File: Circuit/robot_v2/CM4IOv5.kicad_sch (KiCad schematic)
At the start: 1 part, among them J18 Conn_01x12_Pin

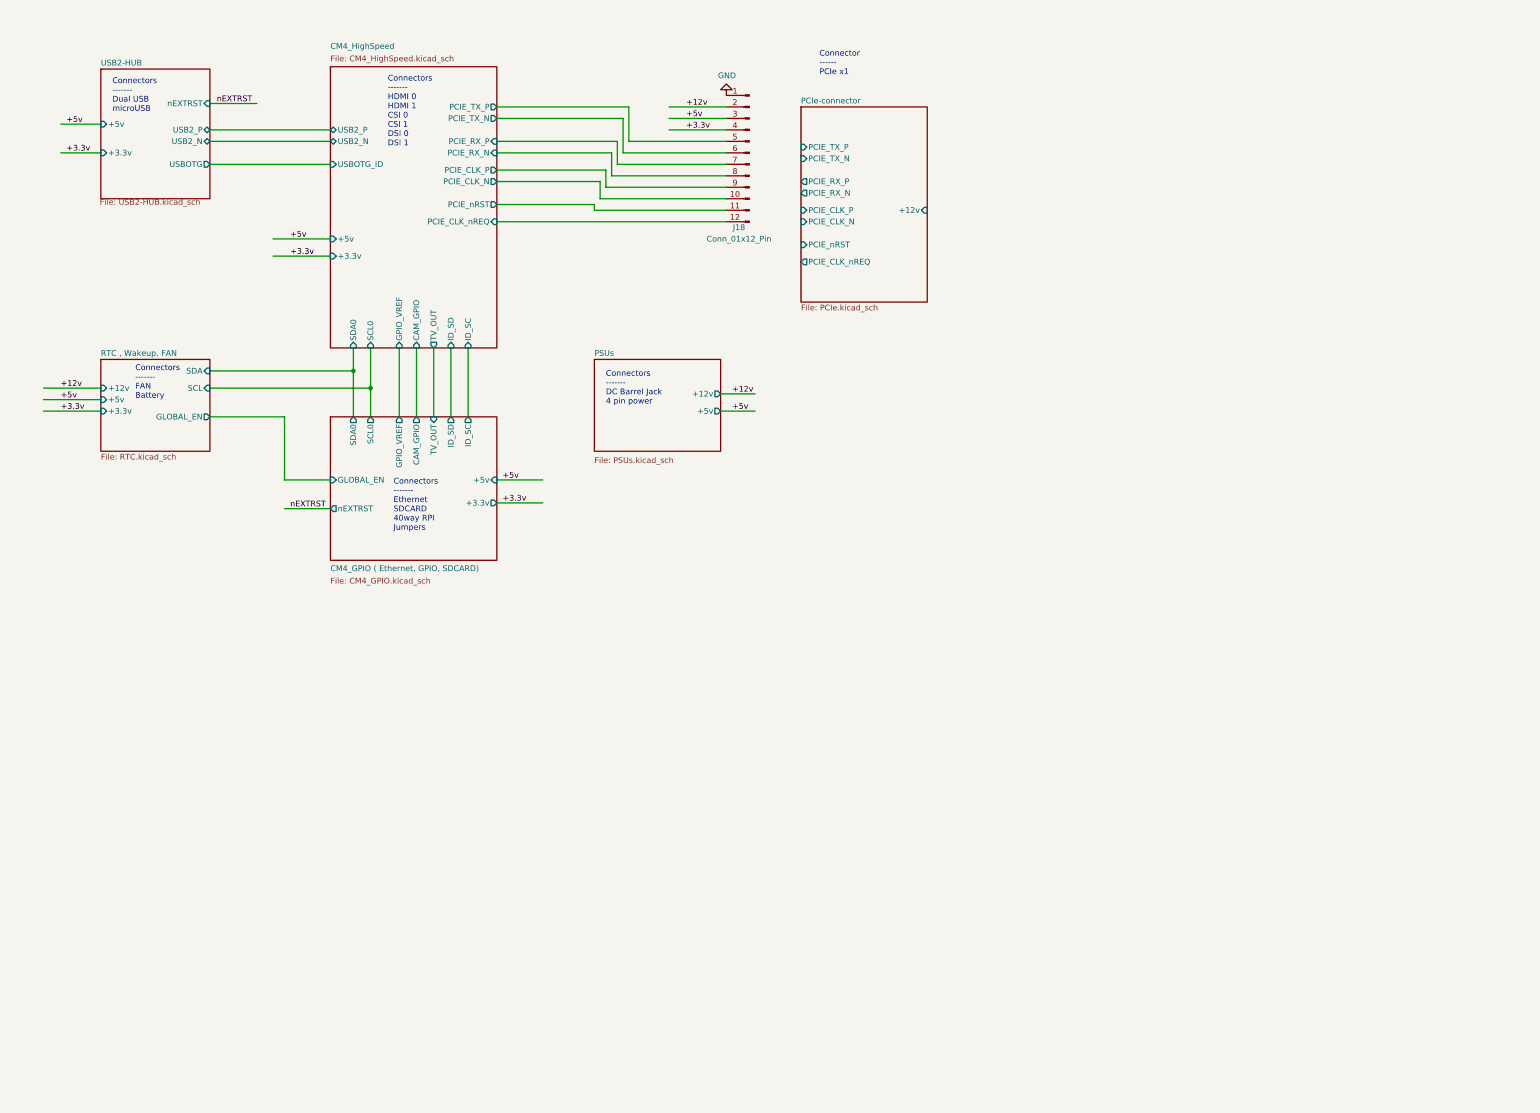
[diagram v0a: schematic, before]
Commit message: feat(kicad): Advance PCB to v0.3 and add EV3 color sensor test
Updates the main robot PCB design to version 0.3 ('Robot fő nyák_v3') with new features and refinements. Simultaneously adds a v0.1 test program for the Lego EV3 color sensor.
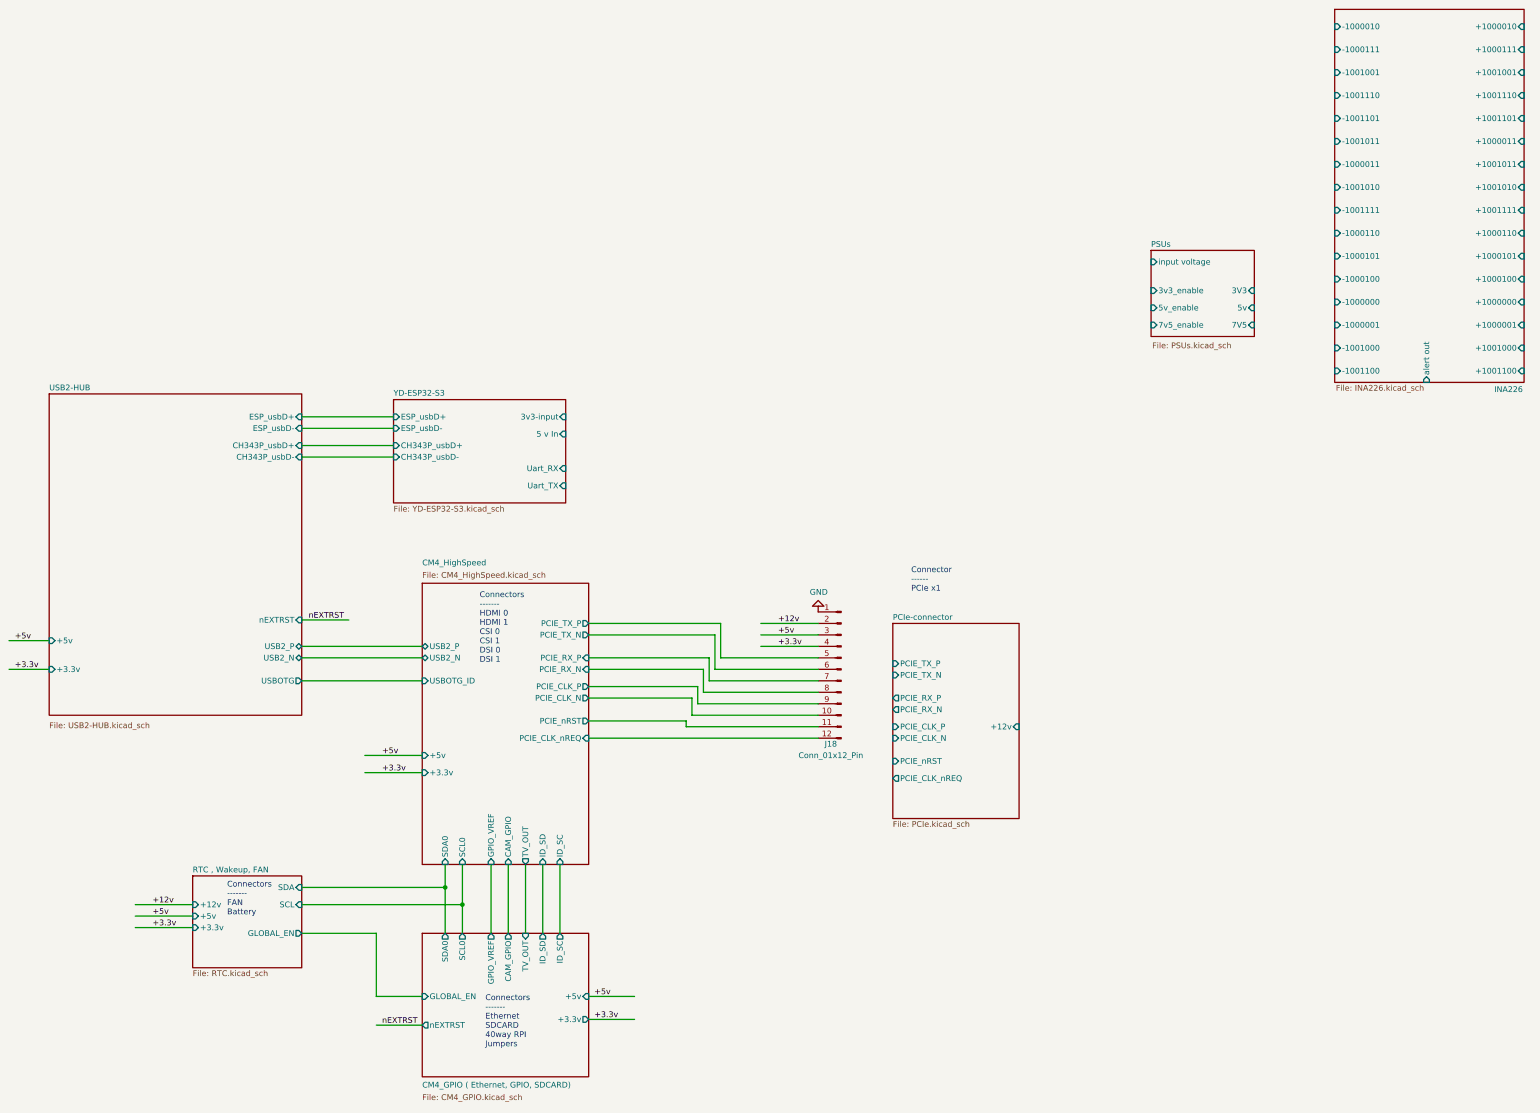
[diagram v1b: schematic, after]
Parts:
- J18: footprint Connector_JST:JST_EH_B12B-EH-A_1x12_P2.50mm_Vertical -> Connector_PinHeader_2.54mm:PinHeader_1x12_P2.54mm_Vertical
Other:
- added sheet INA226 (INA226.kicad_sch)
- added sheet YD-ESP32-S3 (YD-ESP32-S3.kicad_sch)
- sheet PSUs ports: added 3V3, 3v3_enable, 5v, 5v_enable, 7V5, 7v5_enable, input voltage; removed +12v, +5v
- sheet USB2-HUB ports: added CH343P_usbD+, CH343P_usbD-, ESP_usbD+, ESP_usbD-; removed none
- note removed: "Connectors ------- DC Barrel Jack 4 pin power"
- note removed: "Connectors ------- Dual USB microUSB"
- moved on the sheet: J18

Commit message: chore: Update web page and save KiCad progress
This commit includes miscellaneous updates. The project's webpage (`web/index.html`) has been modified, and various KiCad project files have been saved, reflecting ongoing design work.
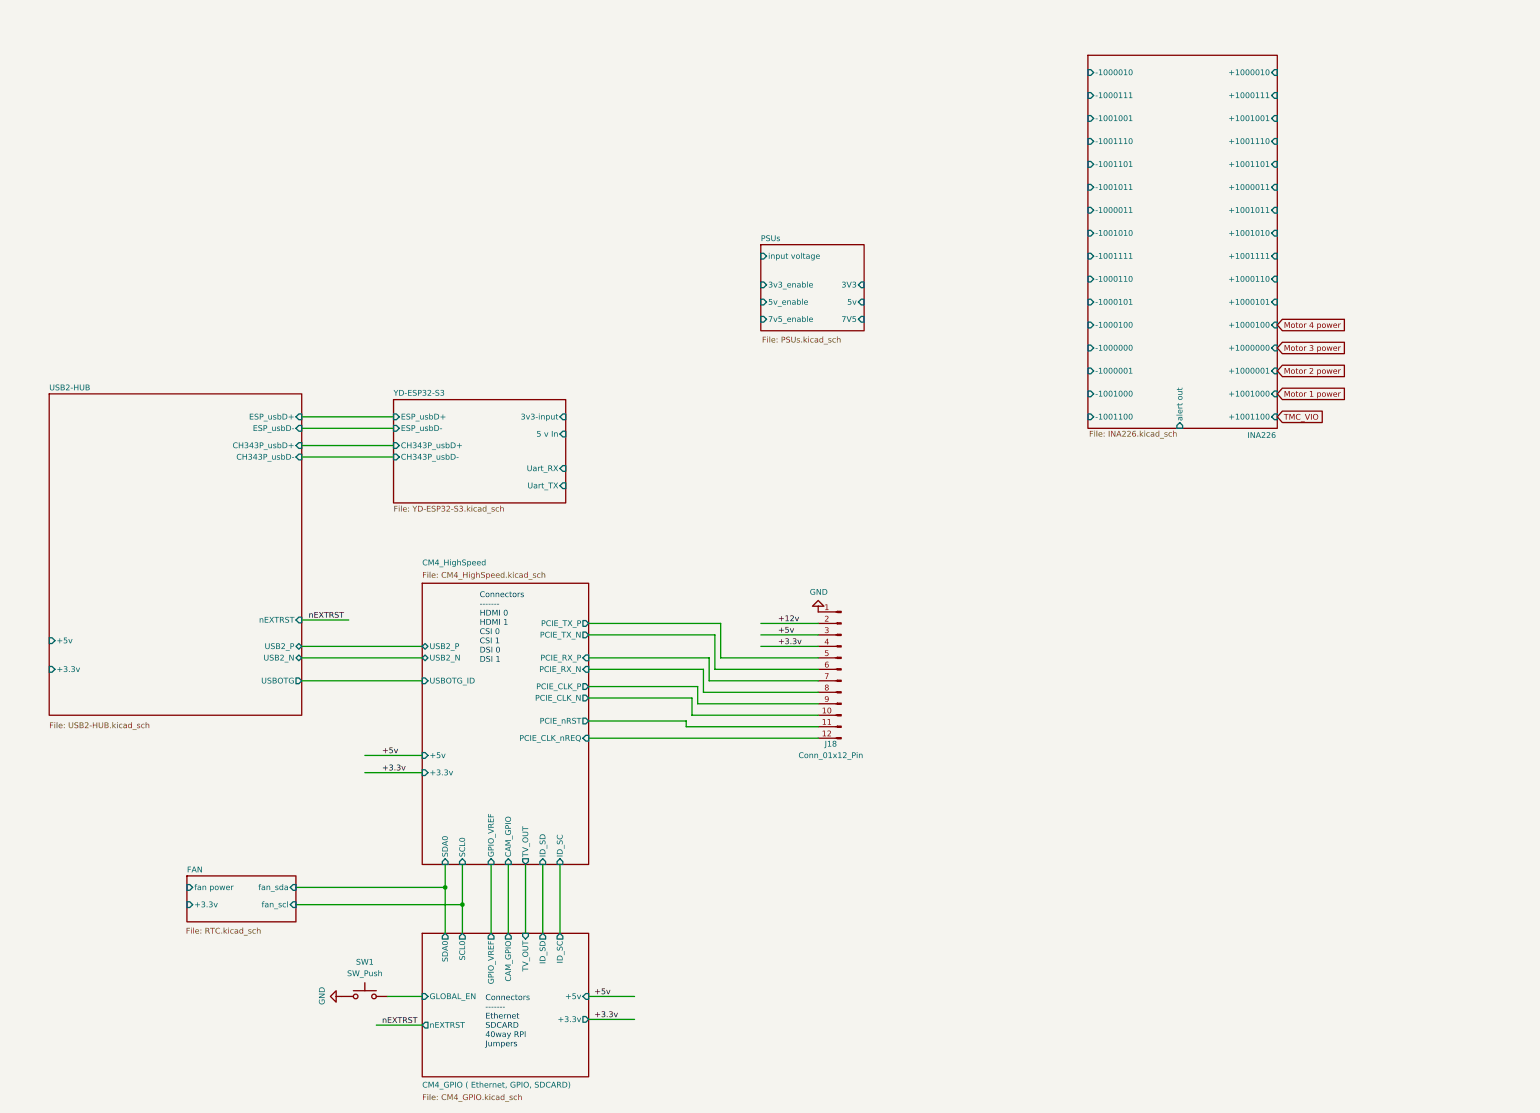
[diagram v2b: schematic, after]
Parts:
- added SW1: SW_Push, symbol Switch:SW_Push
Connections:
- net CM4_GPIO ( Ethernet, GPIO, SDCARD)/GLOBAL_EN: now also SW1.2
- net GND: now also SW1.1
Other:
- sheet RTC , Wakeup, FAN renamed FAN
- removed sheet PCIe-connector
- sheet FAN ports: added fan power, fan_scl, fan_sda; removed +12v, +5v, GLOBAL_EN, SCL, SDA
- note removed: "Connector ------ PCIe x1"
- note removed: "Connectors ------- FAN Battery"
